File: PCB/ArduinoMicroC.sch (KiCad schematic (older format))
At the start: 28 parts, among them J1 USB_C_Receptacle_USB2.0, J2 Conn_01x12, J3 Conn_01x05, J4 Conn_01x12, SW2 SW_Push, U1 MIC5219-5.0YM5, U2 ATmega32U4-M, Y1 16MHz

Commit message: Update Schematic for version 3
Add D+ and D- pins for headers
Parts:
- removed J2, J4: Conn_01x12, NeihConnector:PinHeader_1x12_P2.54mm_Circular_Vertical_2, symbol Connector_Generic:Conn_01x12
- added J2, J4: Conn_01x13, NeihConnector:PinHeader_1x13_P2.54mm_Circular_Vertical_2, symbol Connector_Generic:Conn_01x13
- C1, C3: symbol Device:CP1_Small -> Device:C_Polarized_Small_US
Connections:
- net 10: now also J4.1 (Pin_1)
- net 14: now also J4.3 (Pin_3)
- net 15: now also J4.4 (Pin_4)
- net 16: now also J4.2 (Pin_2)
- net 4: now also J2.8 (Pin_8)
- net 5: now also J2.9 (Pin_9)
- net 6: now also J2.10 (Pin_10)
- net 7: now also J2.11 (Pin_11)
- net 8: now also J2.12 (Pin_12)
- net 9: now also J2.13 (Pin_13)
- net A0: now also J4.5 (Pin_5)
- net A1: now also J4.6 (Pin_6)
- net A2: now also J4.7 (Pin_7)
- net A3: now also J4.8 (Pin_8)
- net D+: now also J1.A6 (D+), J1.B6 (D+), R1.1, J2.1 (Pin_1); no longer R1.2, U2.4 (D+)
- net D-: now also J1.A7 (D-), J1.B7 (D-), R2.1, J4.13 (Pin_13); no longer R2.2, U2.3 (D-)
- net GND: now also J2.4 (Pin_4), J2.5 (Pin_5), J4.11 (Pin_11)
- net RAW: now also J4.12 (Pin_12)
- net RESET: now also J4.10 (Pin_10)
- net RX: now also J2.3 (Pin_3)
- net SCL: now also J2.7 (Pin_7)
- net SDA: now also J2.6 (Pin_6)
- net TX: now also J2.2 (Pin_2)
- net VCC: now also J4.9 (Pin_9)
- new net C_D+: R1.2, U2.4 (D+)
- new net C_D-: R2.2, U2.3 (D-)
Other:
- moved on the sheet: J3, R1, R2
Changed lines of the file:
@@
 GND
 Text GLabel 7250 3400 0    50   Input ~ 0
-D+
+C_D+
 Text GLabel 7250 3500 0    50   Input ~ 0
-D-
+C_D-
 Text GLabel 7250 3200 0    50   Input ~ 0
 VBUS
@@
 Text GLabel 4500 5300 3    50   Input ~ 0
 GND
-Text GLabel 4150 5300 3    50   Input ~ 0
-D-
-Text GLabel 3800 5300 3    50   Input ~ 0
-D+
+Text GLabel 4150 5800 3    50   Input ~ 0
+C_D-
+Text GLabel 3800 5800 3    50   Input ~ 0
+C_D+
 Wire Wire Line
 	4500 5150 4500 5300
 Wire Wire Line
-	4150 5150 4150 5300
-Wire Wire Line
-	3800 5150 3800 5300
+	4150 5650 4150 5800
+Wire Wire Line
+	3800 5650 3800 5800
 Text GLabel 6750 3700 0    50   Input ~ 0
 GND
@@
 $EndComp
 $Comp
-L Device:CP1_Small C3
+L Device:C_Polarized_Small_US C3
 U 1 1 5FBA004F
 P 5350 3200
@@
 $EndComp
 $Comp
-L Device:CP1_Small C1
+L Device:C_Polarized_Small_US C1
 U 1 1 5FBA0049
 P 4000 3200
@@
 L Device:R_Small_US R1
 U 1 1 5FBA0037
-P 3800 5050
-F 0 "R1" H 3868 5096 50  0000 L CNN
-F 1 "5.1K" H 3868 5005 50  0000 L CNN
-F 2 "Resistor_SMD:R_0201_0603Metric" H 3800 5050 50  0001 C CNN
-F 3 "~" H 3800 5050 50  0001 C CNN
-	1    3800 5050
+P 3800 5550
+F 0 "R1" H 3868 5596 50  0000 L CNN
+F 1 "5.1K" H 3868 5505 50  0000 L CNN
+F 2 "Resistor_SMD:R_0201_0603Metric" H 3800 5550 50  0001 C CNN
+F 3 "~" H 3800 5550 50  0001 C CNN
+	1    3800 5550
 	1    0    0    -1
 $EndComp
@@
 L Device:R_Small_US R2
 U 1 1 5FBA002B
-P 4150 5050
-F 0 "R2" H 4218 5096 50  0000 L CNN
-F 1 "5.1K" H 4218 5005 50  0000 L CNN
-F 2 "Resistor_SMD:R_0201_0603Metric" H 4150 5050 50  0001 C CNN
-F 3 "~" H 4150 5050 50  0001 C CNN
-	1    4150 5050
+P 4150 5550
+F 0 "R2" H 4218 5596 50  0000 L CNN
+F 1 "5.1K" H 4218 5505 50  0000 L CNN
+F 2 "Resistor_SMD:R_0201_0603Metric" H 4150 5550 50  0001 C CNN
+F 3 "~" H 4150 5550 50  0001 C CNN
+	1    4150 5550
 	1    0    0    -1
 $EndComp
@@
 Text GLabel 7200 1750 2    50   Input ~ 0
 GND
-$Comp
-L Connector_Generic:Conn_01x12 J2
-U 1 1 5FC6A9ED
-P 5300 4600
-F 0 "J2" H 5380 4592 50  0000 L CNN
-F 1 "Conn_01x12" H 5380 4501 50  0000 L CNN
-F 2 "NeihConnector:PinHeader_1x12_P2.54mm_Circular_Vertical_2" H 5300 4600 50  0001 C CNN
-F 3 "~" H 5300 4600 50  0001 C CNN
-	1    5300 4600
-	1    0    0    -1
-$EndComp
-$Comp
-L Connector_Generic:Conn_01x12 J4
-U 1 1 5FC6B60C
-P 6000 4700
-F 0 "J4" H 5918 3875 50  0000 C CNN
-F 1 "Conn_01x12" H 5918 3966 50  0000 C CNN
-F 2 "NeihConnector:PinHeader_1x12_P2.54mm_Circular_Vertical_2" H 6000 4700 50  0001 C CNN
-F 3 "~" H 6000 4700 50  0001 C CNN
-	1    6000 4700
-	-1   0    0    1
-$EndComp
-Text GLabel 5100 4100 0    50   Input ~ 0
+Text GLabel 5100 4350 0    50   Input ~ 0
 TX
-Text GLabel 5100 4200 0    50   Input ~ 0
+Text GLabel 5100 4450 0    50   Input ~ 0
 RX
-Text GLabel 5100 4300 0    50   Input ~ 0
-GND
-Text GLabel 5100 4400 0    50   Input ~ 0
-GND
-Text GLabel 5100 4500 0    50   Input ~ 0
+Text GLabel 5100 4550 0    50   Input ~ 0
+GND
+Text GLabel 5100 4650 0    50   Input ~ 0
+GND
+Text GLabel 5100 4750 0    50   Input ~ 0
 SDA
-Text GLabel 5100 4600 0    50   Input ~ 0
+Text GLabel 5100 4850 0    50   Input ~ 0
 SCL
-Text GLabel 5100 4700 0    50   Input ~ 0
+Text GLabel 5100 4950 0    50   Input ~ 0
 4
-Text GLabel 5100 4800 0    50   Input ~ 0
+Text GLabel 5100 5050 0    50   Input ~ 0
 5
-Text GLabel 5100 4900 0    50   Input ~ 0
+Text GLabel 5100 5150 0    50   Input ~ 0
 6
-Text GLabel 5100 5000 0    50   Input ~ 0
+Text GLabel 5100 5250 0    50   Input ~ 0
 7
-Text GLabel 5100 5100 0    50   Input ~ 0
+Text GLabel 5100 5350 0    50   Input ~ 0
 8
-Text GLabel 5100 5200 0    50   Input ~ 0
+Text GLabel 5100 5450 0    50   Input ~ 0
 9
-Text GLabel 6200 4100 2    50   Input ~ 0
+Text GLabel 6200 4350 2    50   Input ~ 0
 RAW
-Text GLabel 6200 4200 2    50   Input ~ 0
-GND
-Text GLabel 6200 4300 2    50   Input ~ 0
+Text GLabel 6200 4450 2    50   Input ~ 0
+GND
+Text GLabel 6200 4550 2    50   Input ~ 0
 RESET
-Text GLabel 6200 4400 2    50   Input ~ 0
+Text GLabel 6200 4650 2    50   Input ~ 0
 VCC
-Text GLabel 6200 4500 2    50   Input ~ 0
+Text GLabel 6200 4750 2    50   Input ~ 0
 A3
-Text GLabel 6200 4600 2    50   Input ~ 0
+Text GLabel 6200 4850 2    50   Input ~ 0
 A2
-Text GLabel 6200 4700 2    50   Input ~ 0
+Text GLabel 6200 4950 2    50   Input ~ 0
 A1
-Text GLabel 6200 4800 2    50   Input ~ 0
+Text GLabel 6200 5050 2    50   Input ~ 0
 A0
-Text GLabel 6200 4900 2    50   Input ~ 0
+Text GLabel 6200 5150 2    50   Input ~ 0
 15
-Text GLabel 6200 5000 2    50   Input ~ 0
+Text GLabel 6200 5250 2    50   Input ~ 0
 14
-Text GLabel 6200 5100 2    50   Input ~ 0
+Text GLabel 6200 5350 2    50   Input ~ 0
 16
-Text GLabel 6200 5200 2    50   Input ~ 0
+Text GLabel 6200 5450 2    50   Input ~ 0
 10
-Text GLabel 5450 5400 3    50   Input ~ 0
+Text GLabel 5450 5650 3    50   Input ~ 0
 12
-Text GLabel 5550 5400 3    50   Input ~ 0
+Text GLabel 5550 5650 3    50   Input ~ 0
 13
-Text GLabel 5650 5400 3    50   Input ~ 0
+Text GLabel 5650 5650 3    50   Input ~ 0
 A4
-Text GLabel 5750 5400 3    50   Input ~ 0
+Text GLabel 5750 5650 3    50   Input ~ 0
 A5
-Text GLabel 5850 5400 3    50   Input ~ 0
+Text GLabel 5850 5650 3    50   Input ~ 0
 17
 $Comp
@@
 L Connector_Generic:Conn_01x05 J3
 U 1 1 5FDE6139
-P 5650 5200
-F 0 "J3" V 5614 4912 50  0000 R CNN
-F 1 "Conn_01x05" V 5523 4912 50  0000 R CNN
-F 2 "NeihConnector:PinHeader_1x05_P2.54mm_Circular_Vertical_2" H 5650 5200 50  0001 C CNN
-F 3 "~" H 5650 5200 50  0001 C CNN
-	1    5650 5200
+P 5650 5450
+F 0 "J3" V 5614 5162 50  0000 R CNN
+F 1 "Conn_01x05" V 5523 5162 50  0000 R CNN
+F 2 "NeihConnector:PinHeader_1x05_P2.54mm_Circular_Vertical_2" H 5650 5450 50  0001 C CNN
+F 3 "~" H 5650 5450 50  0001 C CNN
+	1    5650 5450
 	0    -1   -1   0
 $EndComp
@@
 Wire Wire Line
 	4750 2850 5350 2850
+$Comp
+L Connector_Generic:Conn_01x13 J2
+U 1 1 601AFC80
+P 5300 4850
+F 0 "J2" H 5380 4892 50  0000 L CNN
+F 1 "Conn_01x13" H 5380 4801 50  0000 L CNN
+F 2 "NeihConnector:PinHeader_1x13_P2.54mm_Circular_Vertical_2" H 5300 4850 50  0001 C CNN
+F 3 "~" H 5300 4850 50  0001 C CNN
+	1    5300 4850
+	1    0    0    -1
+$EndComp
+$Comp
+L Connector_Generic:Conn_01x13 J4
+U 1 1 601B16C7
+P 6000 4850
+F 0 "J4" H 5918 4025 50  0000 C CNN
+F 1 "Conn_01x13" H 5918 4116 50  0000 C CNN
+F 2 "NeihConnector:PinHeader_1x13_P2.54mm_Circular_Vertical_2" H 6000 4850 50  0001 C CNN
+F 3 "~" H 6000 4850 50  0001 C CNN
+	1    6000 4850
+	-1   0    0    1
+$EndComp
+Text GLabel 5100 4250 0    50   Input ~ 0
+D+
+Text GLabel 6200 4250 2    50   Input ~ 0
+D-
+Text GLabel 3800 4950 3    50   Input ~ 0
+D+
+Text GLabel 4150 4950 3    50   Input ~ 0
+D-
+Wire Wire Line
+	3800 5450 3800 5300
+Wire Wire Line
+	4150 5450 4150 5300
+Text GLabel 3800 5300 1    50   Input ~ 0
+D+
+Text GLabel 4150 5300 1    50   Input ~ 0
+D-
 $EndSCHEMATC

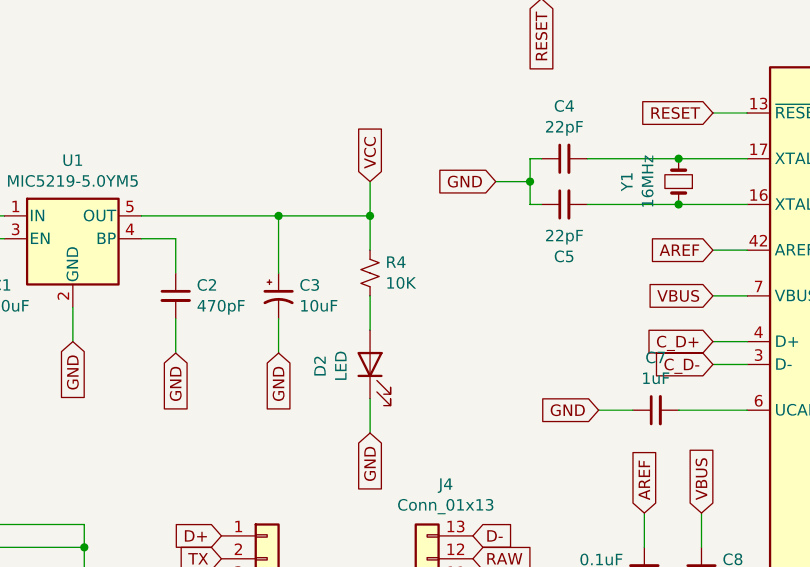
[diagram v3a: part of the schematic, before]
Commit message: Update PCB for version 3
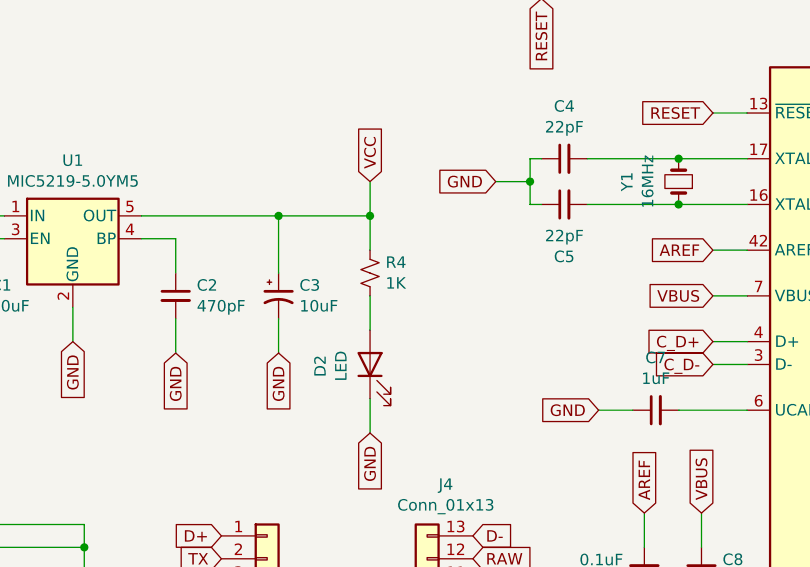
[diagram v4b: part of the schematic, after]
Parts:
- R4: value 10K -> 1K
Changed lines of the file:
@@
 P 5750 3100
 F 0 "R4" H 5818 3146 50  0000 L CNN
-F 1 "10K" H 5818 3055 50  0000 L CNN
+F 1 "1K" H 5818 3055 50  0000 L CNN
 F 2 "Resistor_SMD:R_0201_0603Metric" H 5750 3100 50  0001 C CNN
 F 3 "~" H 5750 3100 50  0001 C CNN

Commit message: Update header J2, J4 and update filled zones
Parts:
- J2, J4: footprint NeihConnector:PinHeader_1x13_P2.54mm_Circular_Vertical_2 -> NeihConnector:PinHeader_1x13_P2.54mm_Circular_Vertical_3
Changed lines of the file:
@@
 F 0 "J2" H 5380 4892 50  0000 L CNN
 F 1 "Conn_01x13" H 5380 4801 50  0000 L CNN
-F 2 "NeihConnector:PinHeader_1x13_P2.54mm_Circular_Vertical_2" H 5300 4850 50  0001 C CNN
+F 2 "NeihConnector:PinHeader_1x13_P2.54mm_Circular_Vertical_3" H 5300 4850 50  0001 C CNN
 F 3 "~" H 5300 4850 50  0001 C CNN
 	1    5300 4850
@@
 F 0 "J4" H 5918 4025 50  0000 C CNN
 F 1 "Conn_01x13" H 5918 4116 50  0000 C CNN
-F 2 "NeihConnector:PinHeader_1x13_P2.54mm_Circular_Vertical_2" H 6000 4850 50  0001 C CNN
+F 2 "NeihConnector:PinHeader_1x13_P2.54mm_Circular_Vertical_3" H 6000 4850 50  0001 C CNN
 F 3 "~" H 6000 4850 50  0001 C CNN
 	1    6000 4850

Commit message: Update headers for PCB
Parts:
- J2, J4: footprint NeihConnector:PinHeader_1x13_P2.54mm_Circular_Vertical_3 -> NeihConnector:PinHeader_1x13_P2.54mm_Circular_Vertical_2
- R4: value 1K -> 4.7K
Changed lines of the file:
@@
 P 5750 3100
 F 0 "R4" H 5818 3146 50  0000 L CNN
-F 1 "1K" H 5818 3055 50  0000 L CNN
+F 1 "4.7K" H 5818 3055 50  0000 L CNN
 F 2 "Resistor_SMD:R_0201_0603Metric" H 5750 3100 50  0001 C CNN
 F 3 "~" H 5750 3100 50  0001 C CNN
@@
 F 0 "J2" H 5380 4892 50  0000 L CNN
 F 1 "Conn_01x13" H 5380 4801 50  0000 L CNN
-F 2 "NeihConnector:PinHeader_1x13_P2.54mm_Circular_Vertical_3" H 5300 4850 50  0001 C CNN
+F 2 "NeihConnector:PinHeader_1x13_P2.54mm_Circular_Vertical_2" H 5300 4850 50  0001 C CNN
 F 3 "~" H 5300 4850 50  0001 C CNN
 	1    5300 4850
@@
 F 0 "J4" H 5918 4025 50  0000 C CNN
 F 1 "Conn_01x13" H 5918 4116 50  0000 C CNN
-F 2 "NeihConnector:PinHeader_1x13_P2.54mm_Circular_Vertical_3" H 6000 4850 50  0001 C CNN
+F 2 "NeihConnector:PinHeader_1x13_P2.54mm_Circular_Vertical_2" H 6000 4850 50  0001 C CNN
 F 3 "~" H 6000 4850 50  0001 C CNN
 	1    6000 4850
